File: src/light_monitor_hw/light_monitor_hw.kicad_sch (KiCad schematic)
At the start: 1 part, among them U1 STM32L433VCTx

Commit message: Setting up outline for schematic
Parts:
- added BT1: 1062, 1062, symbol SamacSys_Parts:1062
- added J1: USB_B_Micro, symbol Connector:USB_B_Micro
- added SW1: SW_SPDT, symbol Switch:SW_SPDT
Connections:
- new net GND: BT1.2 (-)
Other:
- note added: "Battery Source"
- note added: "Regulation Stage"
- note added: "Select Power Source USB source is also OFF unless USB is plugged in"
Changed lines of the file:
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@@
 (kicad_sch (version 20230121) (generator eeschema)
-  (paper "A4")
+  (paper "A3")
   (title_block
     (date "2023-03-26")
     (company "Alexander S. Adranly")
   )
-  (symbol (lib_id "MCU_ST_STM32L4:STM32L433VCTx") (at 124.46 107.95 0) (unit 1)
-    (in_bom yes) (on_board yes) (dnp no) (fields_autoplaced)
-    (property "Reference" "U1" (at 128.9559 176.53 0)
+  (rectangle (start 105.41 102.87) (end 134.62 170.18)
+    (stroke (width 0) (type default))
+    (fill (type none))
+  )
+  (rectangle (start 31.75 102.87) (end 64.77 170.18)
+    (stroke (width 0) (type default))
+    (fill (type none))
+  )
+  (rectangle (start 67.31 102.87) (end 102.87 170.18)
+    (stroke (width 0) (type default))
+    (fill (type none))
+  )
+  (text "Select Power Source\n\nUSB source is also OFF \nunless USB is plugged in"
+    (at 107.95 113.03 0)
+    (effects (font (size 1.27 1.27)) (justify left bottom))
+  )
+  (text "Battery Source" (at 39.37 143.51 0)
+    (effects (font (size 1.27 1.27)) (justify left bottom))
+  )
+  (text "Regulation Stage" (at 76.2 113.03 0)
+    (effects (font (size 1.27 1.27)) (justify left bottom))
+  )
+  (symbol (lib_id "power:GND") (at 45.72 161.29 0) (unit 1)
+    (in_bom yes) (on_board yes) (dnp no) (fields_autoplaced)
+    (property "Reference" "#PWR01" (at 45.72 167.64 0)
+      (effects (font (size 1.27 1.27)) hide)
+    )
+    (property "Value" "GND" (at 45.72 166.37 0)
+      (effects (font (size 1.27 1.27)))
+    )
+    (property "Footprint" "" (at 45.72 161.29 0)
+      (effects (font (size 1.27 1.27)) hide)
+    )
+    (property "Datasheet" "" (at 45.72 161.29 0)
+      (effects (font (size 1.27 1.27)) hide)
+    )
+    (pin "1")
+    (instances
+      (project "light_monitor_hw"
+        (path "/f2c5757f-e0e3-42ec-a3b9-27ce976e3a0f"
+          (reference "#PWR01") (unit 1)
+        )
+      )
+    )
+  )
+  (symbol (lib_id "SamacSys_Parts:1062") (at 45.72 161.29 90) (unit 1)
+    (in_bom yes) (on_board yes) (dnp no) (fields_autoplaced)
+    (property "Reference" "BT1" (at 52.07 150.495 90)
+      (effects (font (size 1.27 1.27)) (justify right))
+    )
+    (property "Value" "1062" (at 52.07 153.035 90)
+      (effects (font (size 1.27 1.27)) (justify right))
+    )
+    (property "Footprint" "1062" (at 43.18 144.78 0)
+      (effects (font (size 1.27 1.27)) (justify left) hide)
+    )
+    (property "Datasheet" "https://www.keyelco.com/product-pdf.cfm?p=728" (at 45.72 144.78 0)
+      (effects (font (size 1.27 1.27)) (justify left) hide)
+    )
+    (property "Description" "KEYSTONE - 1062 - BATTERY HOLDER, 2 CELL, 20MM" (at 48.26 144.78 0)
+      (effects (font (size 1.27 1.27)) (justify left) hide)
+    )
+    (property "Height" "10.57" (at 50.8 144.78 0)
+      (effects (font (size 1.27 1.27)) (justify left) hide)
+    )
+    (property "Manufacturer_Name" "Keystone Electronics" (at 53.34 144.78 0)
+      (effects (font (size 1.27 1.27)) (justify left) hide)
+    )
+    (property "Manufacturer_Part_Number" "1062" (at 55.88 144.78 0)
+      (effects (font (size 1.27 1.27)) (justify left) hide)
+    )
+    (property "Mouser Part Number" "534-1062" (at 58.42 144.78 0)
+      (effects (font (size 1.27 1.27)) (justify left) hide)
+    )
+    (property "Mouser Price/Stock" "https://www.mouser.co.uk/ProductDetail/Keystone-Electronics/1062?qs=TMDrOSIpnUdOWsMNtyKpVg%3D%3D" (at 60.96 144.78 0)
+      (effects (font (size 1.27 1.27)) (justify left) hide)
+    )
+    (property "Arrow Part Number" "" (at 63.5 144.78 0)
+      (effects (font (size 1.27 1.27)) (justify left) hide)
+    )
+    (property "Arrow Price/Stock" "" (at 66.04 144.78 0)
+      (effects (font (size 1.27 1.27)) (justify left) hide)
+    )
+    (pin "1")
+    (pin "2")
+    (instances
+      (project "light_monitor_hw"
+        (path "/f2c5757f-e0e3-42ec-a3b9-27ce976e3a0f"
+          (reference "BT1") (unit 1)
+        )
+      )
+    )
+  )
+  (symbol (lib_id "MCU_ST_STM32L4:STM32L433VCTx") (at 234.95 167.64 0) (unit 1)
+    (in_bom yes) (on_board yes) (dnp no) (fields_autoplaced)
+    (property "Reference" "U1" (at 239.4459 236.22 0)
       (effects (font (size 1.27 1.27)) (justify left))
     )
-    (property "Value" "STM32L433VCTx" (at 128.9559 179.07 0)
+    (property "Value" "STM32L433VCTx" (at 239.4459 238.76 0)
       (effects (font (size 1.27 1.27)) (justify left))
     )
-    (property "Footprint" "Package_QFP:LQFP-100_14x14mm_P0.5mm" (at 106.68 173.99 0)
+    (property "Footprint" "Package_QFP:LQFP-100_14x14mm_P0.5mm" (at 217.17 233.68 0)
       (effects (font (size 1.27 1.27)) (justify right) hide)
     )
-    (property "Datasheet" "https://www.st.com/resource/en/datasheet/stm32l433vc.pdf" (at 124.46 107.95 0)
+    (property "Datasheet" "https://www.st.com/resource/en/datasheet/stm32l433vc.pdf" (at 234.95 167.64 0)
       (effects (font (size 1.27 1.27)) hide)
     )
@@
         )
       )
+    )
+  )
+  (symbol (lib_id "Switch:SW_SPDT") (at 118.11 139.7 180) (unit 1)
+    (in_bom yes) (on_board yes) (dnp no) (fields_autoplaced)
+    (property "Reference" "SW1" (at 118.11 133.35 0)
+      (effects (font (size 1.27 1.27)))
+    )
+    (property "Value" "SW_SPDT" (at 118.11 135.89 0)
+      (effects (font (size 1.27 1.27)))
+    )
+    (property "Footprint" "" (at 118.11 139.7 0)
+      (effects (font (size 1.27 1.27)) hide)
+    )
+    (property "Datasheet" "~" (at 118.11 139.7 0)
+      (effects (font (size 1.27 1.27)) hide)
+    )
+    (pin "1")
+    (pin "2")
+    (pin "3")
+    (instances
+      (project "light_monitor_hw"
+        (path "/f2c5757f-e0e3-42ec-a3b9-27ce976e3a0f"
+          (reference "SW1") (unit 1)
+        )
+      )
+    )
+  )
+  (symbol (lib_id "Connector:USB_B_Micro") (at 46.99 119.38 0) (unit 1)
+    (in_bom yes) (on_board yes) (dnp no) (fields_autoplaced)
+    (property "Reference" "J1" (at 46.99 107.95 0)
+      (effects (font (size 1.27 1.27)))
+    )
+    (property "Value" "USB_B_Micro" (at 46.99 110.49 0)
+      (effects (font (size 1.27 1.27)))
+    )
+    (property "Footprint" "" (at 50.8 120.65 0)
+      (effects (font (size 1.27 1.27)) hide)
+    )
+    (property "Datasheet" "~" (at 50.8 120.65 0)
+      (effects (font (size 1.27 1.27)) hide)
+    )
+    (pin "1")
+    (pin "2")
+    (pin "3")
+    (pin "4")
+    (pin "5")
+    (pin "6")
+    (instances
+      (project "light_monitor_hw"
+        (path "/f2c5757f-e0e3-42ec-a3b9-27ce976e3a0f"
+          (reference "J1") (unit 1)
+        )
+      )

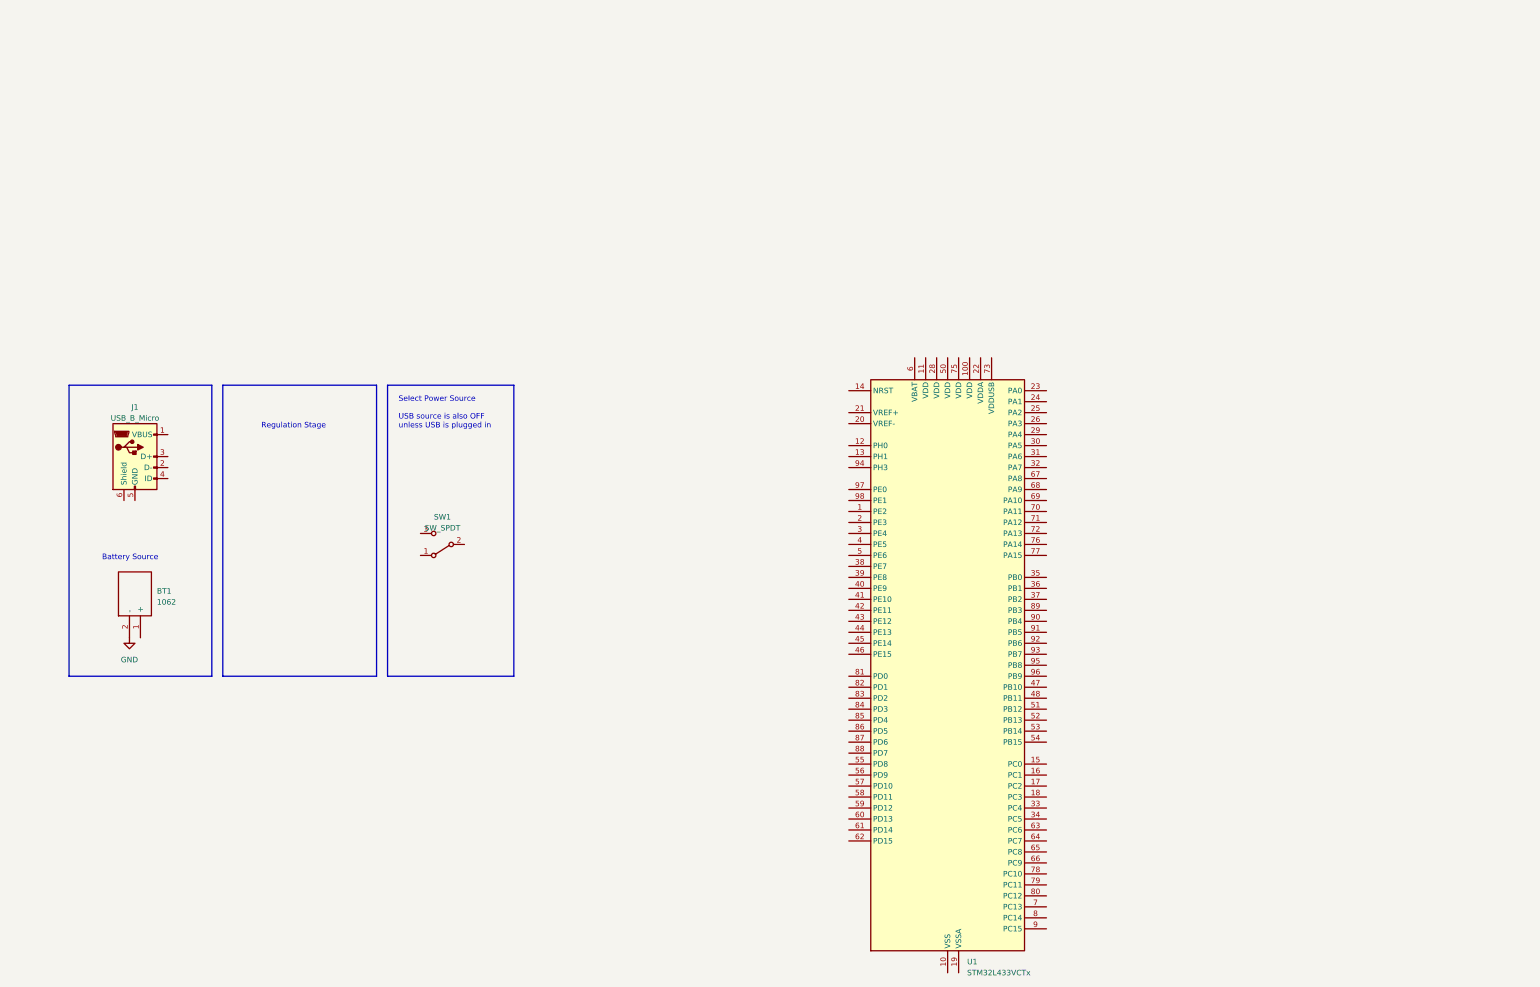
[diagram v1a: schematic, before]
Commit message: Added voltage regulation ICs for battery and USB power
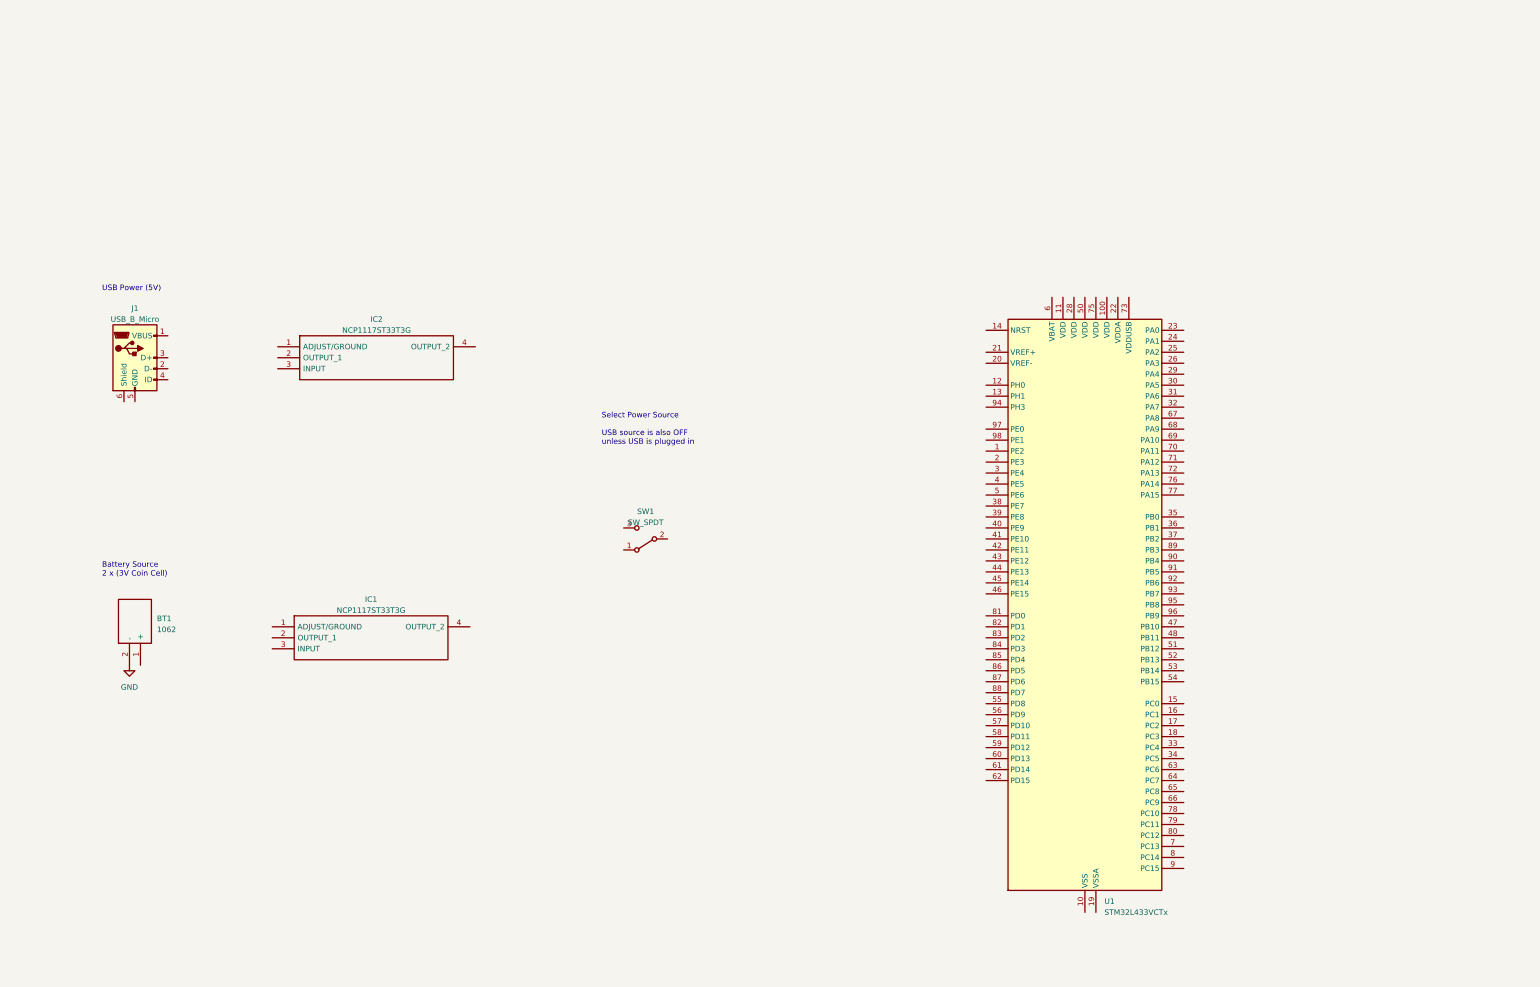
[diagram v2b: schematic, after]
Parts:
- added IC1, IC2: NCP1117ST33T3G, SOT230P700X180-4N, symbol SamacSys_Parts:NCP1117ST33T3G
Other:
- note added: "Battery Source 2 x (3V Coin Cell)"
- note added: "USB Power (5V)"
- note removed: "Battery Source"
- note removed: "Regulation Stage"
- moved on the sheet: BT1, J1, SW1, U1

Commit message: Adding all major components to schematic
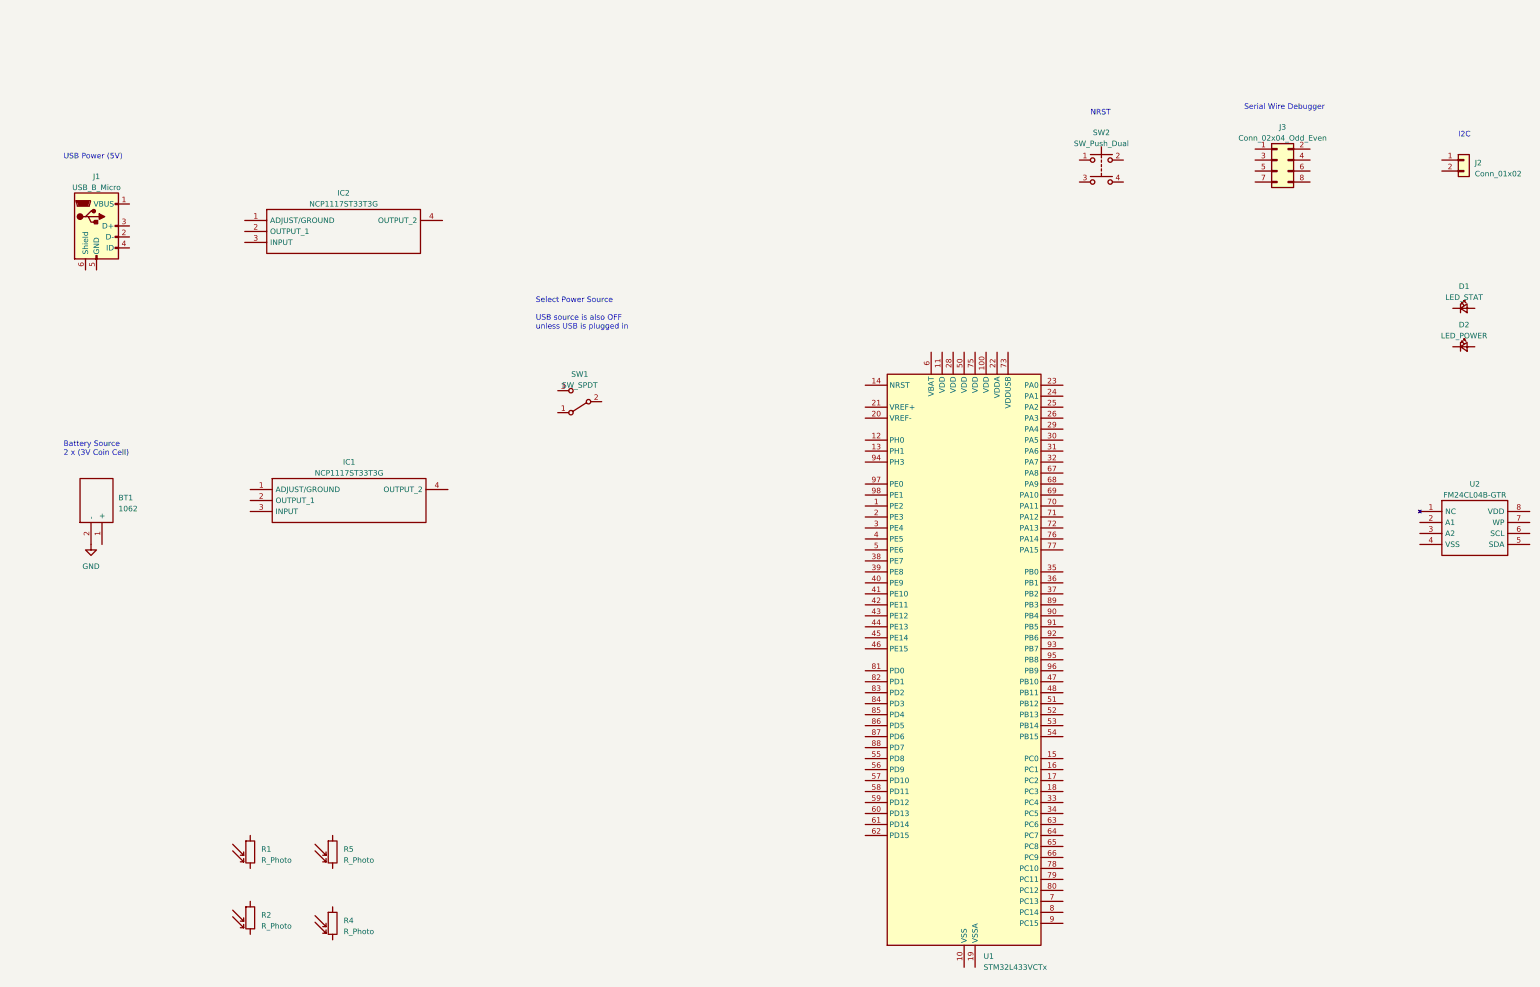
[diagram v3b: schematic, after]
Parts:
- added D1: LED_STAT, symbol Device:LED_Small
- added D2: LED_POWER, symbol Device:LED_Small
- added J2: Conn_01x02, symbol Connector_Generic:Conn_01x02
- added J3: Conn_02x04_Odd_Even, symbol Connector_Generic:Conn_02x04_Odd_Even
- added R1, R2, R4, R5: R_Photo, symbol Device:R_Photo
- added SW2: SW_Push_Dual, symbol Switch:SW_Push_Dual
- added U2: FM24CL04B-GTR, SOIC127P602X173-8N, symbol SamacSys_Parts:FM24CL04B-GTR
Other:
- note added: "I2C"
- note added: "NRST"
- note added: "Serial Wire Debugger"
- moved on the sheet: BT1, IC1, IC2, J1, SW1, U1

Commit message: [schematic] divided into different sheets, high-level power supply
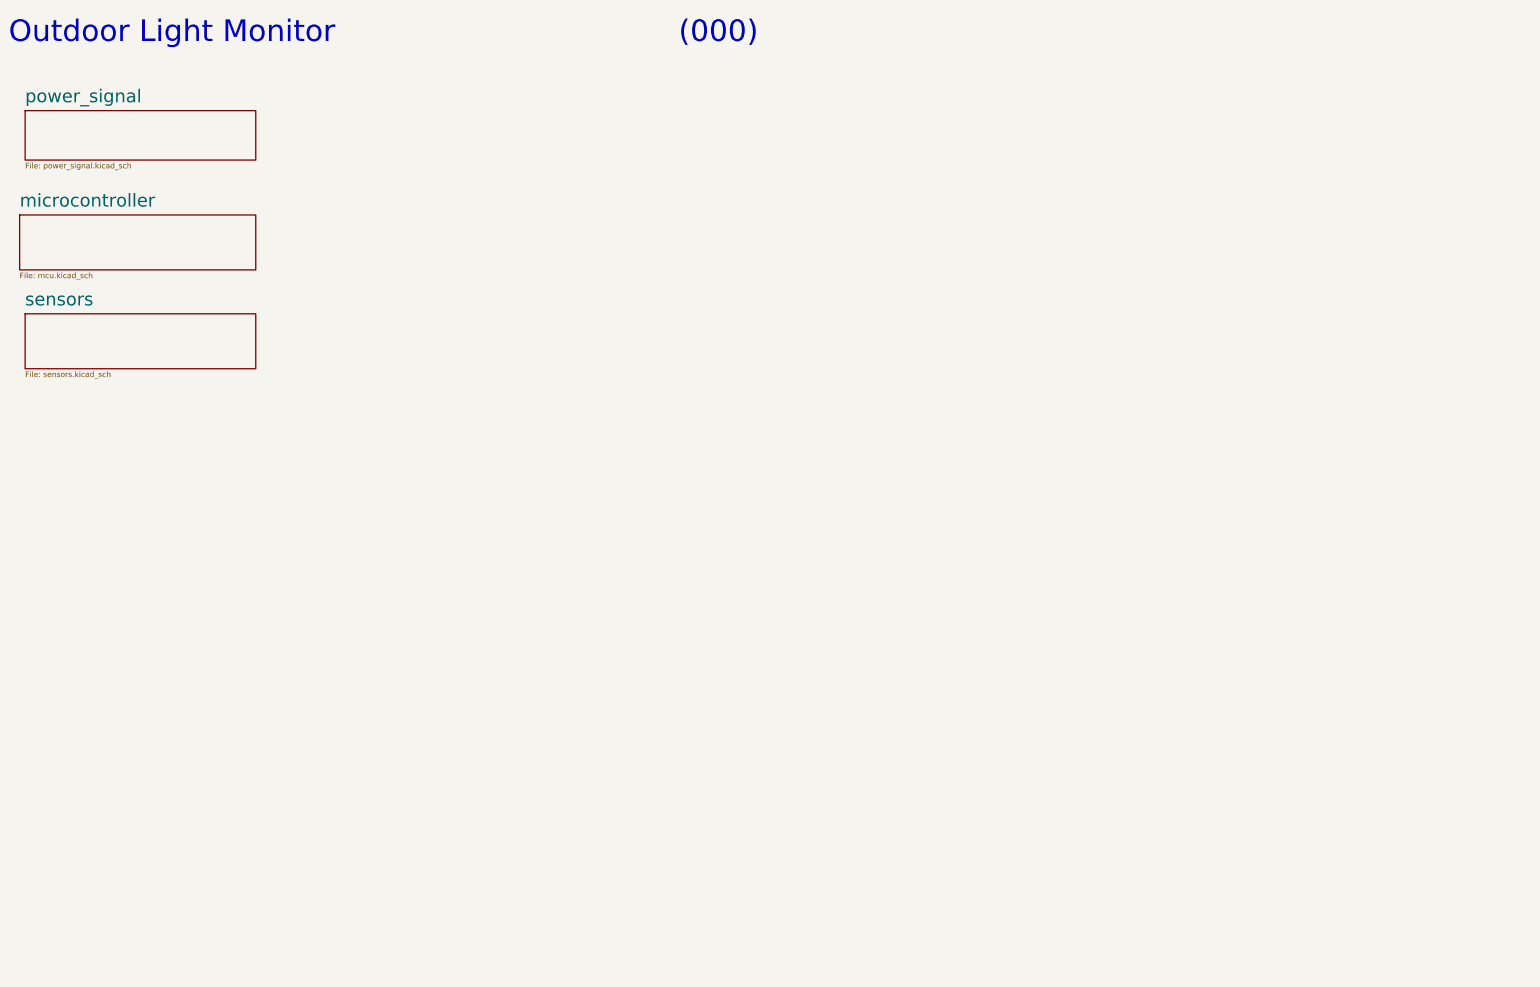
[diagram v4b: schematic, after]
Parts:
- removed BT1: 1062, 1062, symbol SamacSys_Parts:1062
- removed D1: LED_STAT, symbol Device:LED_Small
- removed D2: LED_POWER, symbol Device:LED_Small
- removed IC1, IC2: NCP1117ST33T3G, SOT230P700X180-4N, symbol SamacSys_Parts:NCP1117ST33T3G
- removed J1: USB_B_Micro, symbol Connector:USB_B_Micro
- removed J2: Conn_01x02, symbol Connector_Generic:Conn_01x02
- removed J3: Conn_02x04_Odd_Even, symbol Connector_Generic:Conn_02x04_Odd_Even
- removed R1, R2, R4, R5: R_Photo, symbol Device:R_Photo
- removed SW1: SW_SPDT, symbol Switch:SW_SPDT
- removed SW2: SW_Push_Dual, symbol Switch:SW_Push_Dual
- removed U1: STM32L433VCTx, Package_QFP:LQFP-100_14x14mm_P0.5mm, symbol MCU_ST_STM32L4:STM32L433VCTx
- removed U2: FM24CL04B-GTR, SOIC127P602X173-8N, symbol SamacSys_Parts:FM24CL04B-GTR
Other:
- added sheet microcontroller (mcu.kicad_sch)
- added sheet power_signal (power_signal.kicad_sch)
- added sheet sensors (sensors.kicad_sch)
- note added: "(000)"
- note added: "Outdoor Light Monitor"
- note removed: "Battery Source 2 x (3V Coin Cell)"
- note removed: "I2C"
- note removed: "NRST"
- note removed: "Select Power Source USB source is also OFF unless USB is plugged in"
- note removed: "Serial Wire Debugger"
- note removed: "USB Power (5V)"
